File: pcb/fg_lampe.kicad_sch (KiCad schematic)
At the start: 55 parts, among them J1 ISP Port, J2 I^{2}C Debug, J3 RX/TX, J4 PWR Control, J5 1792863, J6 1792863, J7 1792863, Q7 IRLZ540N, Q8 IRLZ540N, SW1 Reset Button, U1 ATmega328P-P, U12 MIC4427, U2 L7805, U3 MAX1044, U4 MAX1044, U5 MCP4812, U8 MCP3008, Y1 16MHz

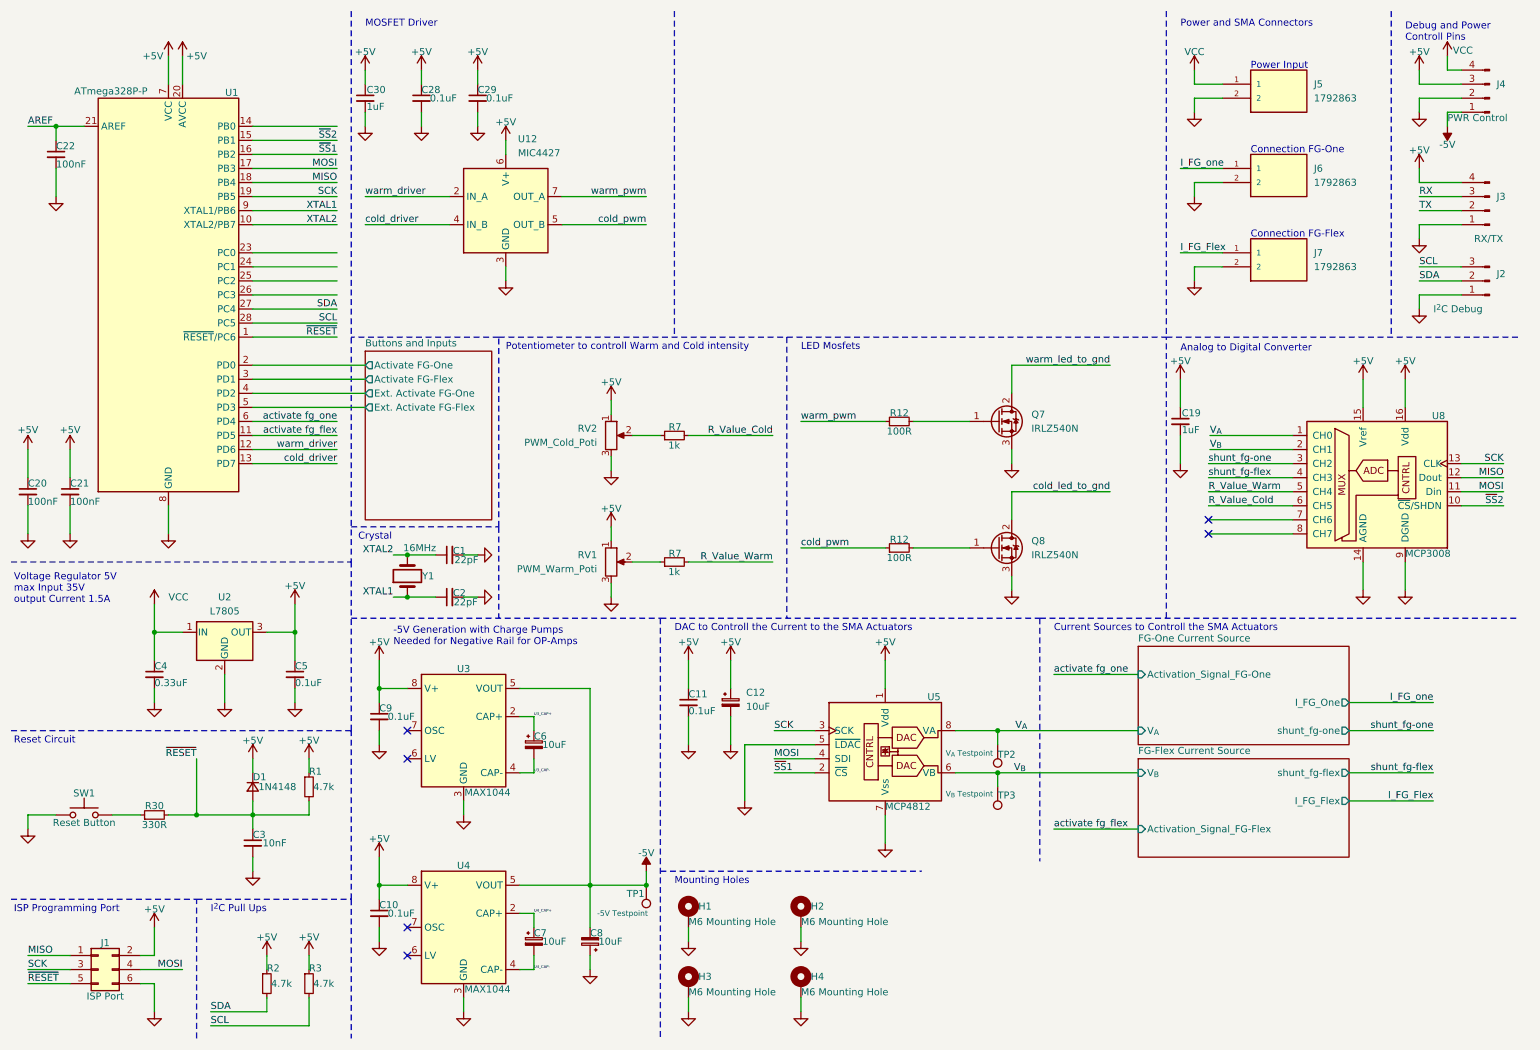
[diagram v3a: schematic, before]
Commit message: vcc changed with +24V
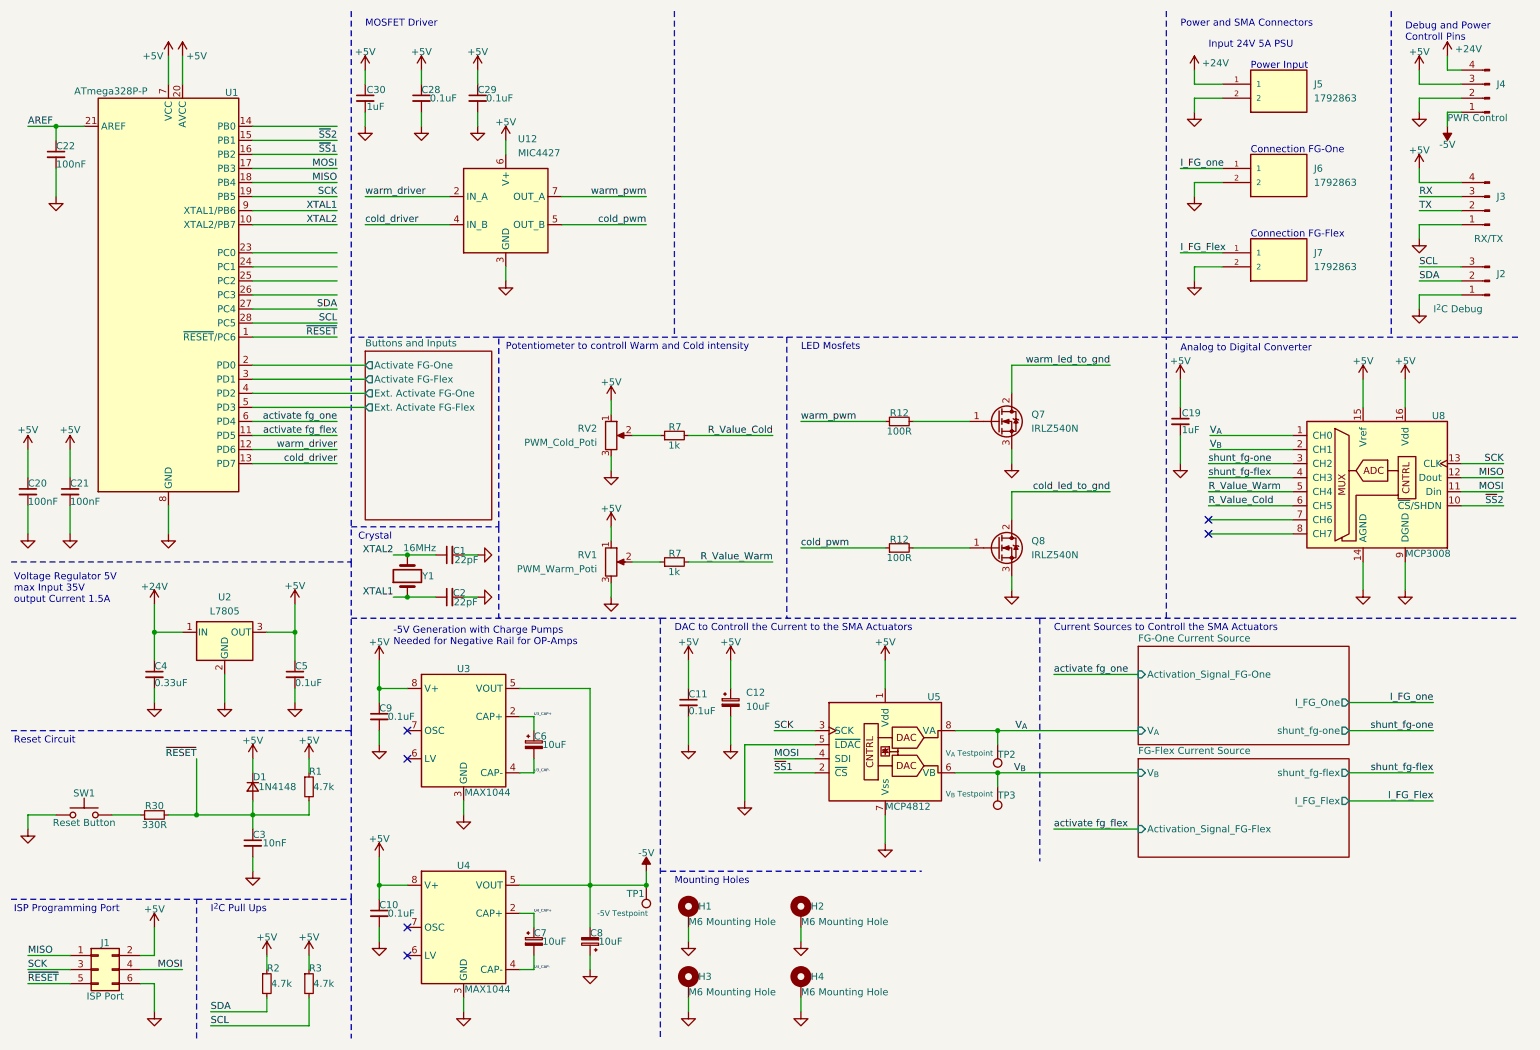
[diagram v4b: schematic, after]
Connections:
- net VCC renamed +24V
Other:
- note added: "Input 24V 5A PSU"
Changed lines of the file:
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@@
     (effects (font (size 1.27 1.27)) (justify left bottom))
   )
+  (text "Input 24V 5A PSU" (at 228.6 19.05 0)
+    (effects (font (size 1.27 1.27)) (justify left bottom))
+  )
   (text "LED Mosfets\n" (at 154.94 73.66 0)
     (effects (font (size 1.27 1.27)) (justify left bottom))
@@
     )
   )
+  (symbol (lib_id "power:+24V") (at 226.06 22.86 0) (unit 1)
+    (in_bom yes) (on_board yes) (dnp no)
+    (property "Reference" "#PWR046" (at 226.06 26.67 0)
+      (effects (font (size 1.27 1.27)) hide)
+    )
+    (property "Value" "+24V" (at 229.87 21.59 0)
+      (effects (font (size 1.27 1.27)))
+    )
+    (property "Footprint" "" (at 226.06 22.86 0)
+      (effects (font (size 1.27 1.27)) hide)
+    )
+    (property "Datasheet" "" (at 226.06 22.86 0)
+      (effects (font (size 1.27 1.27)) hide)
+    )
+    (pin "1")
+    (instances
+      (project "fg_lampe"
+        (path "/6ce7d73a-8297-412b-a1cf-6113d41486fd/1320187d-24fd-4fe0-8f0e-0b43909d8592"
+          (reference "#PWR046") (unit 1)
+        )
+        (path "/6ce7d73a-8297-412b-a1cf-6113d41486fd"
+          (reference "#PWR072") (unit 1)
+        )
+      )
+    )
+  )
   (symbol (lib_id "power:+5V") (at 40.64 20.32 0) (unit 1)
     (in_bom yes) (on_board yes) (dnp no)
@@
     )
   )
+  (symbol (lib_id "power:+24V") (at 38.1 119.38 0) (unit 1)
+    (in_bom yes) (on_board yes) (dnp no)
+    (property "Reference" "#PWR046" (at 38.1 123.19 0)
+      (effects (font (size 1.27 1.27)) hide)
+    )
+    (property "Value" "+24V" (at 38.1 116.205 0)
+      (effects (font (size 1.27 1.27)))
+    )
+    (property "Footprint" "" (at 38.1 119.38 0)
+      (effects (font (size 1.27 1.27)) hide)
+    )
+    (property "Datasheet" "" (at 38.1 119.38 0)
+      (effects (font (size 1.27 1.27)) hide)
+    )
+    (pin "1")
+    (instances
+      (project "fg_lampe"
+        (path "/6ce7d73a-8297-412b-a1cf-6113d41486fd/1320187d-24fd-4fe0-8f0e-0b43909d8592"
+          (reference "#PWR046") (unit 1)
+        )
+        (path "/6ce7d73a-8297-412b-a1cf-6113d41486fd"
+          (reference "#PWR012") (unit 1)
+        )
+      )
+    )
+  )
   (symbol (lib_id "Device:R_Small") (at 172.72 86.36 90) (unit 1)
     (in_bom yes) (on_board yes) (dnp no)
@@
     )
   )
-  (symbol (lib_id "power:VCC") (at 271.78 20.32 0) (unit 1)
-    (in_bom yes) (on_board yes) (dnp no)
-    (property "Reference" "#PWR0104" (at 271.78 24.13 0)
-      (effects (font (size 1.27 1.27)) hide)
-    )
-    (property "Value" "VCC" (at 274.574 19.304 0)
-      (effects (font (size 1.27 1.27)))
-    )
-    (property "Footprint" "" (at 271.78 20.32 0)
-      (effects (font (size 1.27 1.27)) hide)
-    )
-    (property "Datasheet" "" (at 271.78 20.32 0)
-      (effects (font (size 1.27 1.27)) hide)
-    )
-    (pin "1")
-    (instances
-      (project "fg_lampe"
-        (path "/6ce7d73a-8297-412b-a1cf-6113d41486fd"
-          (reference "#PWR0104") (unit 1)
-        )
-      )
-    )
-  )
   (symbol (lib_id "power:+5V") (at 170.18 129.54 0) (unit 1)
     (in_bom yes) (on_board yes) (dnp no)
@@
     )
   )
-  (symbol (lib_id "power:VCC") (at 226.06 22.86 0) (unit 1)
-    (in_bom yes) (on_board yes) (dnp no)
-    (property "Reference" "#PWR072" (at 226.06 26.67 0)
-      (effects (font (size 1.27 1.27)) hide)
-    )
-    (property "Value" "VCC" (at 226.06 19.558 0)
-      (effects (font (size 1.27 1.27)))
-    )
-    (property "Footprint" "" (at 226.06 22.86 0)
-      (effects (font (size 1.27 1.27)) hide)
-    )
-    (property "Datasheet" "" (at 226.06 22.86 0)
-      (effects (font (size 1.27 1.27)) hide)
-    )
-    (pin "1")
-    (instances
-      (project "fg_lampe"
-        (path "/6ce7d73a-8297-412b-a1cf-6113d41486fd"
-          (reference "#PWR072") (unit 1)
-        )
-      )
-    )
-  )
   (symbol (lib_id "power:GND") (at 40.64 106.68 0) (unit 1)
     (in_bom yes) (on_board yes) (dnp no) (fields_autoplaced)
@@
     )
   )
-  (symbol (lib_id "power:VCC") (at 38.1 119.38 0) (unit 1)
-    (in_bom yes) (on_board yes) (dnp no) (fields_autoplaced)
-    (property "Reference" "#PWR012" (at 38.1 123.19 0)
-      (effects (font (size 1.27 1.27)) hide)
-    )
-    (property "Value" "VCC" (at 40.64 118.11 0)
-      (effects (font (size 1.27 1.27)) (justify left))
-    )
-    (property "Footprint" "" (at 38.1 119.38 0)
-      (effects (font (size 1.27 1.27)) hide)
-    )
-    (property "Datasheet" "" (at 38.1 119.38 0)
-      (effects (font (size 1.27 1.27)) hide)
-    )
-    (pin "1")
-    (instances
-      (project "fg_lampe"
-        (path "/6ce7d73a-8297-412b-a1cf-6113d41486fd"
-          (reference "#PWR012") (unit 1)
-        )
-      )
-    )
-  )
   (symbol (lib_id "power:+5V") (at 266.7 22.86 0) (unit 1)
     (in_bom yes) (on_board yes) (dnp no)
@@
         )
       )
+    )
+  )
+  (symbol (lib_id "power:+24V") (at 271.78 20.32 0) (unit 1)
+    (in_bom yes) (on_board yes) (dnp no)
+    (property "Reference" "#PWR046" (at 271.78 24.13 0)
+      (effects (font (size 1.27 1.27)) hide)
+    )
+    (property "Value" "+24V" (at 275.59 19.05 0)
+      (effects (font (size 1.27 1.27)))
+    )
+    (property "Footprint" "" (at 271.78 20.32 0)
+      (effects (font (size 1.27 1.27)) hide)
+    )
+    (property "Datasheet" "" (at 271.78 20.32 0)
+      (effects (font (size 1.27 1.27)) hide)
+    )
+    (pin "1")
+    (instances
+      (project "fg_lampe"
+        (path "/6ce7d73a-8297-412b-a1cf-6113d41486fd/1320187d-24fd-4fe0-8f0e-0b43909d8592"
+          (reference "#PWR046") (unit 1)
+        )
+        (path "/6ce7d73a-8297-412b-a1cf-6113d41486fd"
+          (reference "#PWR094") (unit 1)
+        )
+      )

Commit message: minor changes
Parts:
- RV1, RV2: footprint (none) -> Connector_JST:JST_EH_B3B-EH-A_1x03_P2.50mm_Vertical
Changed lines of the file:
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@@
       (effects (font (size 1.27 1.27)) (justify right))
     )
-    (property "Footprint" "" (at 120.65 111.76 0)
+    (property "Footprint" "Connector_JST:JST_EH_B3B-EH-A_1x03_P2.50mm_Vertical" (at 120.65 111.76 0)
       (effects (font (size 1.27 1.27)) hide)
     )
@@
       (effects (font (size 1.27 1.27)) (justify right))
     )
-    (property "Footprint" "" (at 120.65 88.9 0)
-      (effects (font (size 1.27 1.27)) hide)
-    )
+    (property "Footprint" "Connector_JST:JST_EH_B3B-EH-A_1x03_P2.50mm_Vertical" (at 120.65 88.9 0)
+      (effects (font (size 1.27 1.27)) hide)
+    )

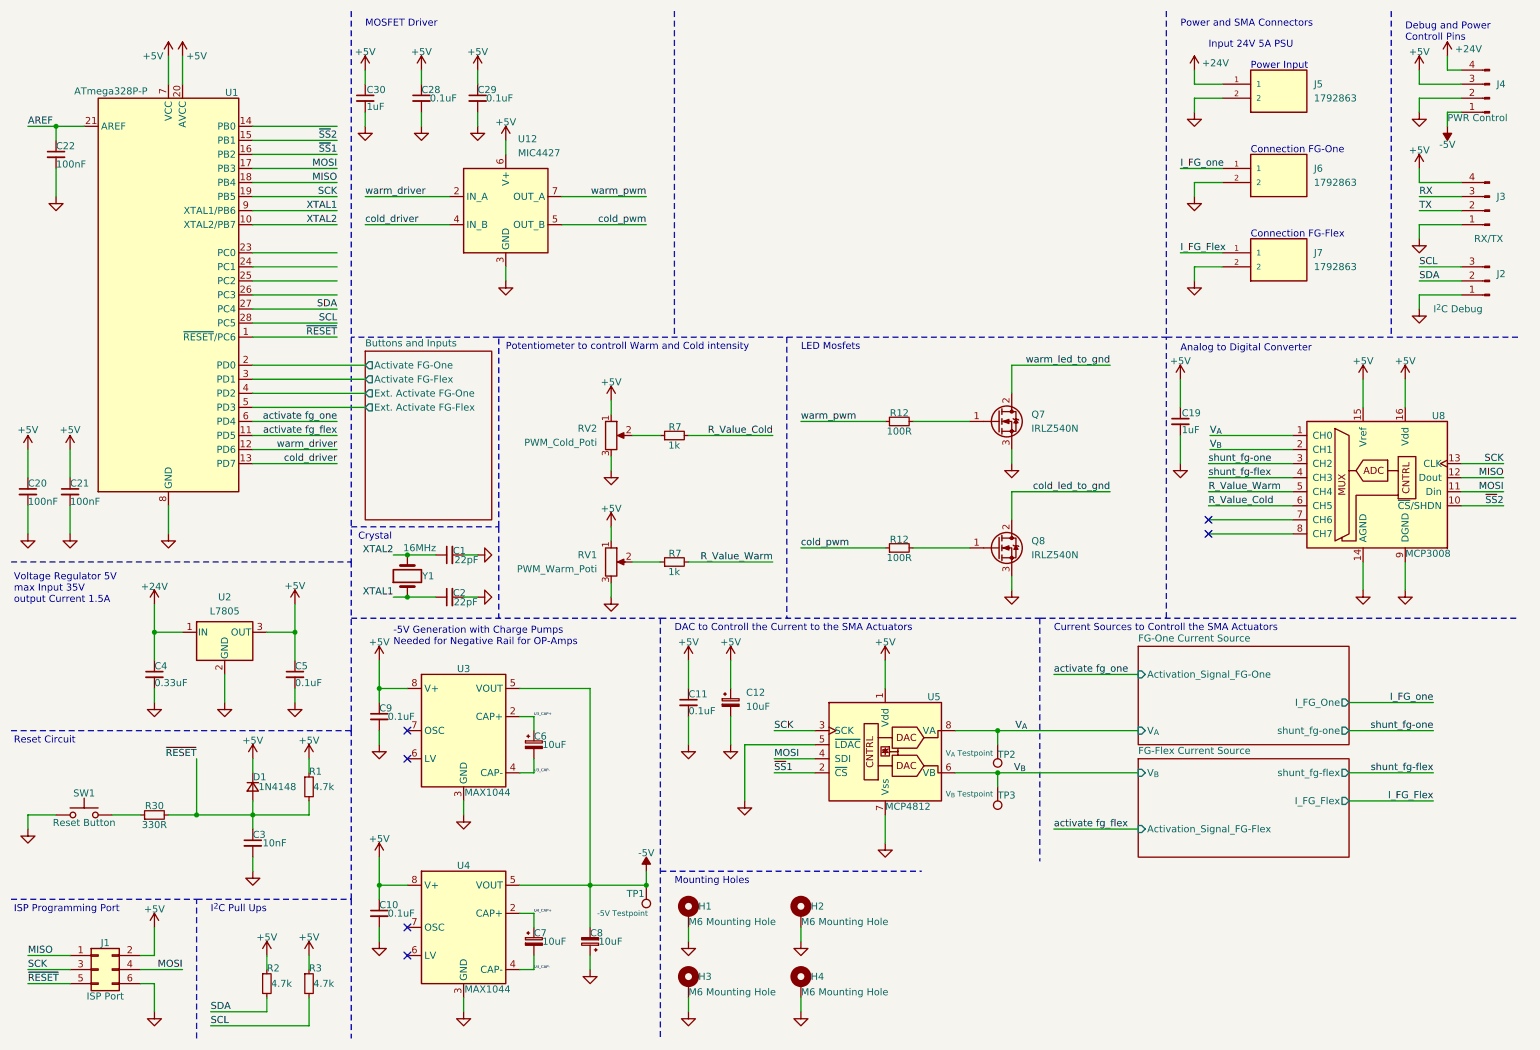
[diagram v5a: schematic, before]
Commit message: sma measurement added, new connector for leds, some minor fixes
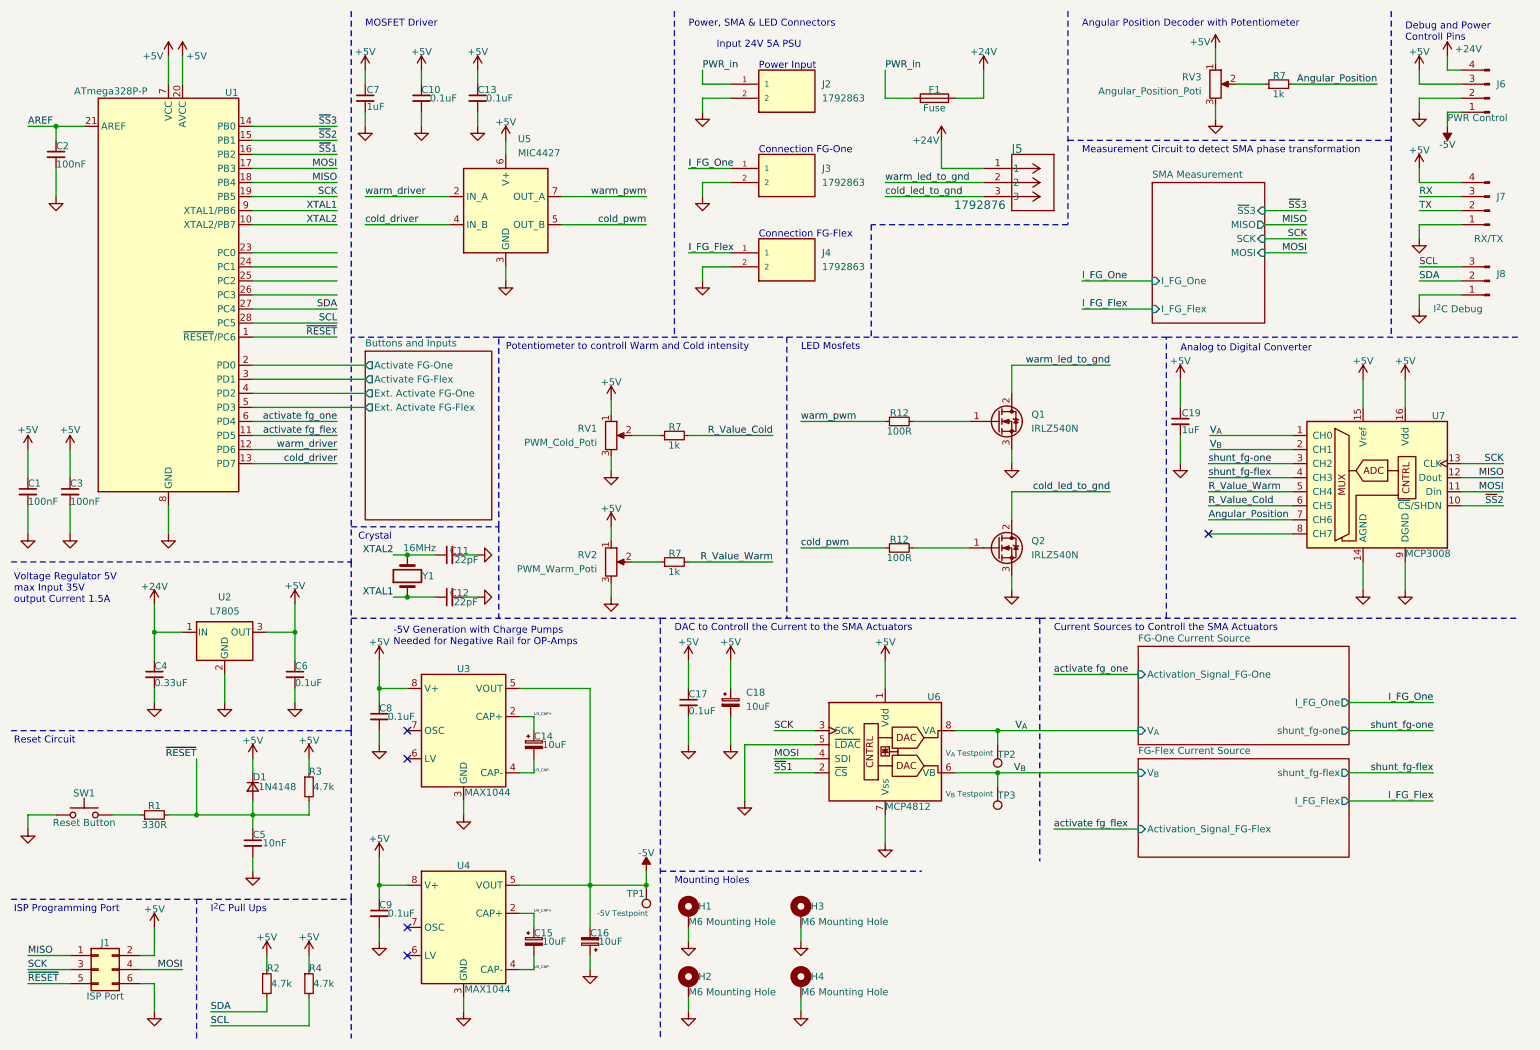
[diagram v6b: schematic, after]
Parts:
- added F1: Fuse, Fuse:Fuseholder_Cylinder-5x20mm_Schurter_0031_8201_Horizontal_Open, symbol Device:Fuse
- added J5: 1792876, phoenic_contact_connector_3_pin:CONN_1792876_PXC, symbol COMBICON PTS Connector 3 Pin:1792876
- added R7: 1k, Resistor_THT:R_Axial_DIN0207_L6.3mm_D2.5mm_P10.16mm_Horizontal, symbol Device:R_Small
- added RV3: Angular_Position_Poti, Connector_JST:JST_EH_B3B-EH-A_1x03_P2.50mm_Vertical, symbol Device:R_Potentiometer
- renumbered C20 to C1, C28 to C10, C1 to C11, C2 to C12, C29 to C13, C6 to C14, C7 to C15, C8 to C16, C11 to C17, C12 to C18, C22 to C2, C21 to C3, C3 to C5, C5 to C6, C30 to C7, C9 to C8, C10 to C9, H3 to H2, H2 to H3, J5 to J2, J6 to J3, J7 to J4, J4 to J6, J3 to J7, J2 to J8, Q7 to Q1, Q8 to Q2, R30 to R1, R1 to R3, R3 to R4, RV2 to RV1, RV1 to RV2, U12 to U5, U5 to U6, U8 to U7
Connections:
- net +24V: now also F1.2, J5.1; no longer J2.1
- net +5V: now also RV3.1
- net GND: now also RV3.3
- net cold_led_to_gnd: now also J5.3
- net warm_led_to_gnd: now also J5.2
- net ~{SS}3: now reaches U1.14 (PB0)
- net Angular_Position: now reaches U7.7 (CH6)
- net Angular_Position: now also R7.2
- net I_FG_one renamed I_FG_One
- new net: R7.1, RV3.2
- new net PWR_in: F1.1, J2.1
- no-connect marks 6 -> 5
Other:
- added sheet SMA Measurement (sma_measurement.kicad_sch)
- note added: "Angular Position Decoder with Potentiometer"
- note added: "Measurement Circuit to detect SMA phase transformation"
- note added: "Power, SMA & LED Connectors"
- note removed: "Power and SMA Connectors"
- moved on the sheet: J2, J3, J4

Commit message: final version schematic?
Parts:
- removed TP1: -5V Testpoint, TestPoint:TestPoint_Pad_D1.0mm, symbol Connector:TestPoint
- added D18, D19: LED, LED_THT:LED_D3.0mm, symbol Device:LED
- added J11: SPI Debug Pins, Connector_PinHeader_2.54mm:PinHeader_1x07_P2.54mm_Vertical, symbol Connector:Conn_01x07_Pin
- added R12 (x2): 220R, Resistor_THT:R_Axial_DIN0207_L6.3mm_D2.5mm_P10.16mm_Horizontal, symbol Device:R_Small
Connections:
- net Buttons and Inputs/Activate FG-Flex: now also U1.5 (PD3); no longer U1.3 (PD1)
- net Buttons and Inputs/Activate FG-One: now also U1.4 (PD2); no longer U1.2 (PD0)
- net Buttons and Inputs/Ext. Activate FG-Flex: now also U1.11 (PD5); no longer U1.5 (PD3)
- net Buttons and Inputs/Ext. Activate FG-One: now also U1.6 (PD4); no longer U1.4 (PD2)
- net GND: now also D18.1 (K), D19.1 (K), J11.1 (Pin_1)
- net MISO: now also J11.3 (Pin_3)
- net MOSI: now also J11.4 (Pin_4)
- net RX: now also U1.2 (PD0)
- net SCK: now also J11.2 (Pin_2)
- net TX: now also U1.3 (PD1)
- net activate fg_flex: now also U1.25 (PC2); no longer U1.11 (PD5)
- net activate fg_one: now also U1.26 (PC3); no longer U1.6 (PD4)
- net ~{SS}1: now also J11.7 (Pin_7)
- net ~{SS}2: now also J11.6 (Pin_6)
- net ~{SS}3: now also J11.5 (Pin_5)
- net LED1: now reaches U1.23 (PC0)
- net LED1: now also R12.1
- net LED2: now reaches U1.24 (PC1)
- net LED2: now also R12.1
- new net: D18.2 (A), R12.2
- new net: D19.2 (A), R12.2
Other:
- note added: "Debug LED's"
- note added: "SPI Debug Pins"
- company: (none) -> /dev/tal e.V.
- moved on the sheet: U5
